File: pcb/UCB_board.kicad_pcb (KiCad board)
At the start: 4 copper layers, 160 x 100 mm, 141 parts, among them IC1 SN65HVD75DR, J1 DIN41612_02x32_AC, J2 TC2030, J3 Conn_01x02_Pin, T1 H1102NL, U1 W5500, U3 USBLC6-2SC6, U4 USBLC6-2SC6, U5 USBLC6-2SC6, U6 FM24C64B, U7 STM32H563VITx, Y1 3225-25M-SR, Y2 3225-25M-SR

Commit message: New power design
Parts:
- added C21: 10u, Capacitor_SMD:C_1206_3216Metric_Pad1.33x1.80mm_HandSolder, F.Cu at (205.9, 62.0)
- added C22: 10u, Capacitor_SMD:C_1206_3216Metric_Pad1.33x1.80mm_HandSolder, F.Cu at (210.9, 62.0)
- added C23: 100n, Capacitor_SMD:C_0603_1608Metric_Pad1.08x0.95mm_HandSolder, F.Cu at (195.8, 67.5)
- added C24: 100n, Capacitor_SMD:C_0603_1608Metric_Pad1.08x0.95mm_HandSolder, F.Cu at (197.3, 67.5)
- added C25: 10u, Capacitor_SMD:C_1206_3216Metric_Pad1.33x1.80mm_HandSolder, F.Cu at (190.7, 67.1)
- added C26: 100n, Capacitor_SMD:C_0603_1608Metric_Pad1.08x0.95mm_HandSolder, F.Cu at (195.1, 63.9)
- added D8: D_TVS, Diode_SMD:D_MiniMELF, B.Cu at (192.3, 62.0)
- added D9: ?, Diode_SMD:D_SMF, B.Cu at (191.9, 58.2)
- added F3: Polyfuse, Fuse:Fuse_1206_3216Metric_Pad1.42x1.75mm_HandSolder, B.Cu at (196.3, 58.3)
- C34: value 100n -> 10u; footprint Capacitor_SMD:C_0603_1608Metric_Pad1.08x0.95mm_HandSolder -> Capacitor_SMD:C_1206_3216Metric_Pad1.33x1.80mm_HandSolder
- D10, D11, D12, F2: moved to B.Cu
- L1: value B82464P4105M000 -> LQH32PN101MN0L; footprint Inductor_SMD:L_10.4x10.4_H4.8 -> Inductor_SMD:L_1210_3225Metric
- moved J2 37.7 mm to (212.5, 93.4)
- moved C33 27.3 mm to (191.8, 63.9), turned to 180 degrees
- moved C43 25.4 mm to (191.9, 58.1), turned to 90 degrees
- moved C42 19.0 mm to (217.2, 67.5), turned to 90 degrees
- moved C47 18.7 mm to (210.9, 59.6), turned to 180 degrees
- moved C48 18.3 mm to (215.8, 62.0), turned to 0 degrees
- moved L1 17.5 mm to (193.5, 66.9), turned to 90 degrees
- moved D10 17.4 mm to (211.7, 59.7), turned to 180 degrees
- moved C31 16.9 mm to (200.9, 62.0), turned to 180 degrees
- moved C41 16.9 mm to (215.7, 67.5), turned to 90 degrees
- moved C46 16.4 mm to (215.0, 63.9), turned to 0 degrees
- moved D11 16.4 mm to (200.9, 62.0), turned to 0 degrees
- moved F2 14.8 mm to (216.2, 58.3)
- moved C44 14.3 mm to (210.6, 67.1)
- moved L3 14.2 mm to (213.3, 66.9)
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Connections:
- C33 pad 1: Net-(C33-Pad1) -> Net-(D8-A2)
- C34 pad 1: Net-(C33-Pad1) -> Net-(D8-A2)
- C36 pad 1: Net-(C33-Pad1) -> Net-(D8-A2)
- C43 pad 1: +3.3V -> Net-(D8-A2)
- L1 pad 1: Net-(C33-Pad1) -> +12V
- L1 pad 2: Net-(D11-A2) -> Net-(D8-A2)
- L2 pad 2: Net-(C33-Pad1) -> Net-(D11-A2)
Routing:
- net /ConnectorDIN41612/PSU/+5V_IN: track 0.00 -> 37.8 mm, vias 0 -> 5
- net /ConnectorDIN41612/PSU/+12V_IN: track 0.00 -> 36.4 mm, vias 0 -> 5
- net /ConnectorDIN41612/PSU/+3,3V_IN: track 0.00 -> 33.5 mm, vias 0 -> 5
- net /ConnectorDIN41612/PSU/-12V_IN: track 0.00 -> 5.08 mm
- net Net-(D8-A2): vias 0 -> 5
- net Net-(D11-A2): vias 0 -> 5
- net Net-(D10-K): vias 0 -> 5
- net GND: vias 11 -> 12
- added copper zone on B.Cu, net /ConnectorDIN41612/PSU/+12V_IN
- added copper zone on In1.Cu, net /ConnectorDIN41612/PSU/+12V_IN
- added copper zone on B.Cu, net /ConnectorDIN41612/PSU/+3,3V_IN
- added copper zone on In1.Cu, net /ConnectorDIN41612/PSU/+3,3V_IN
- added copper zone on B.Cu, net /ConnectorDIN41612/PSU/+5V_IN
- added copper zone on In1.Cu, net /ConnectorDIN41612/PSU/+5V_IN
- added copper zone on B.Cu, net Net-(D10-K)
- added copper zone on F.Cu, net Net-(D10-K)
- added copper zone on B.Cu, net Net-(D8-A2)
- added copper zone on F.Cu, net Net-(D8-A2)
- removed copper zone on F.Cu, net Net-(C33-Pad1)

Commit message: Update
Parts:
- C53: moved to B.Cu
- moved C35 65.8 mm to (193.5, 110.2), turned to 90 degrees
- moved C29 62.3 mm to (191.9, 96.2), turned to -90 degrees
- moved C27 56.2 mm to (197.9, 92.4), turned to 180 degrees
- moved C53 48.5 mm to (202.5, 93.6), turned to -90 degrees
- moved C54 47.5 mm to (209.6, 111.6), turned to 180 degrees
- moved C49 46.2 mm to (205.9, 92.5), turned to 180 degrees
- moved C55 45.6 mm to (209.6, 110.1), turned to 180 degrees
- moved C50 42.5 mm to (209.5, 94.1), turned to -90 degrees
- moved TP3 9.58 mm to (215.6, 104.2)
- moved TP4 4.93 mm to (211.8, 104.3)
- moved TP12 1.30 mm to (203.5, 113.6)
- moved R91 1.02 mm to (211.8, 101.8)
- moved C20 0.05 mm to (199.5, 89.9)
- moved R20 0.05 mm to (201.7, 92.5)
- moved C19 0.05 mm to (204.0, 89.9)
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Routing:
- net GND: track 29.9 -> 58.5 mm, vias 12 -> 15
- net +3.3V: track 31.3 -> 59.3 mm, vias 16 -> 19
- net /MCU/nRESET: track 0.00 -> 23.4 mm, vias 0 -> 2
- net /MCU/SWDIO: track 0.00 -> 21.7 mm, vias 0 -> 2
- net /MCU/SWCLK: track 0.00 -> 20.5 mm, vias 0 -> 2
- net /MCU/SWO: track 0.00 -> 12.2 mm, vias 0 -> 2
- net /MCU/BOOT: track 0.00 -> 10.4 mm
- net /MCU/XTAL-: track 0.00 -> 6.00 mm
- net /MCU/XTAL+: track 0.00 -> 5.99 mm
- net /ConnectorDIN41612/RxD: track 4.99 -> 6.61 mm
- net /MCU/SDA: track 0.00 -> 1.35 mm, vias 0 -> 1
- net /ConnectorDIN41612/TxD: track 12.5 -> 13.3 mm, vias 0 -> 1

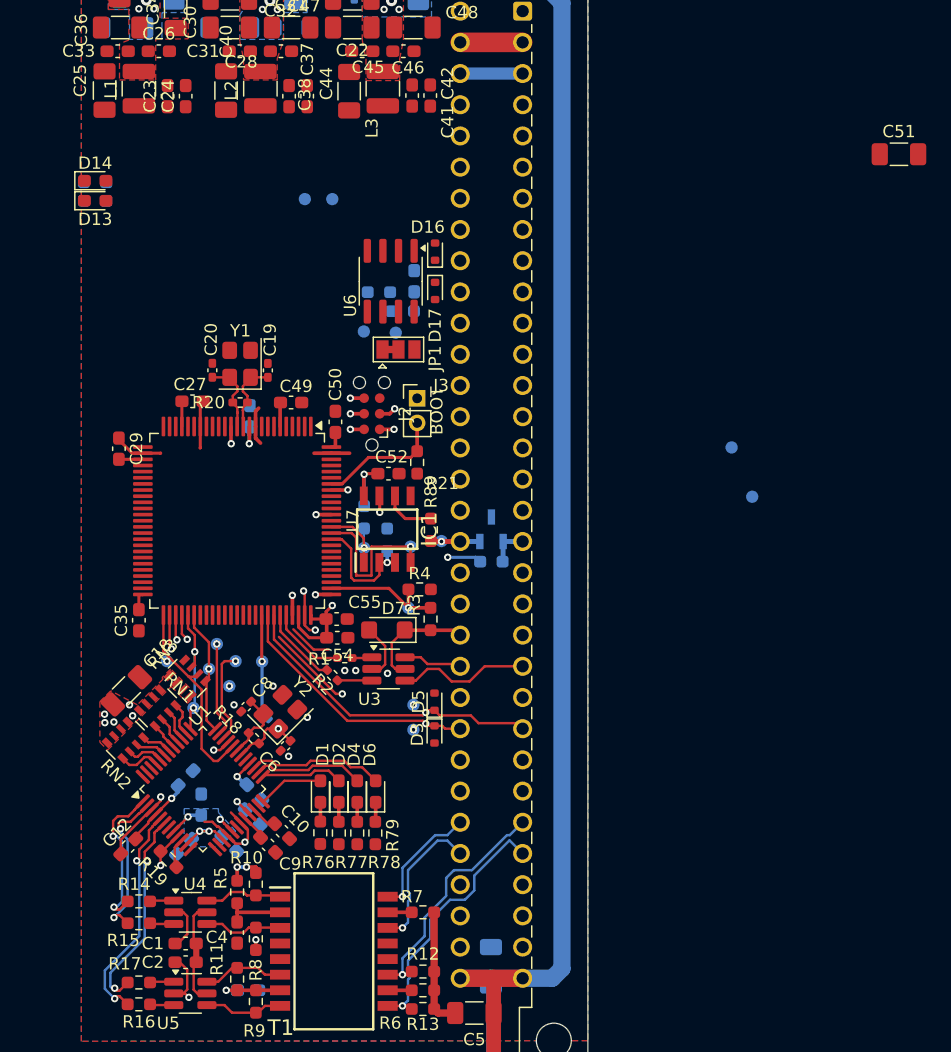
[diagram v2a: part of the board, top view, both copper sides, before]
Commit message: Add connections and new footprints
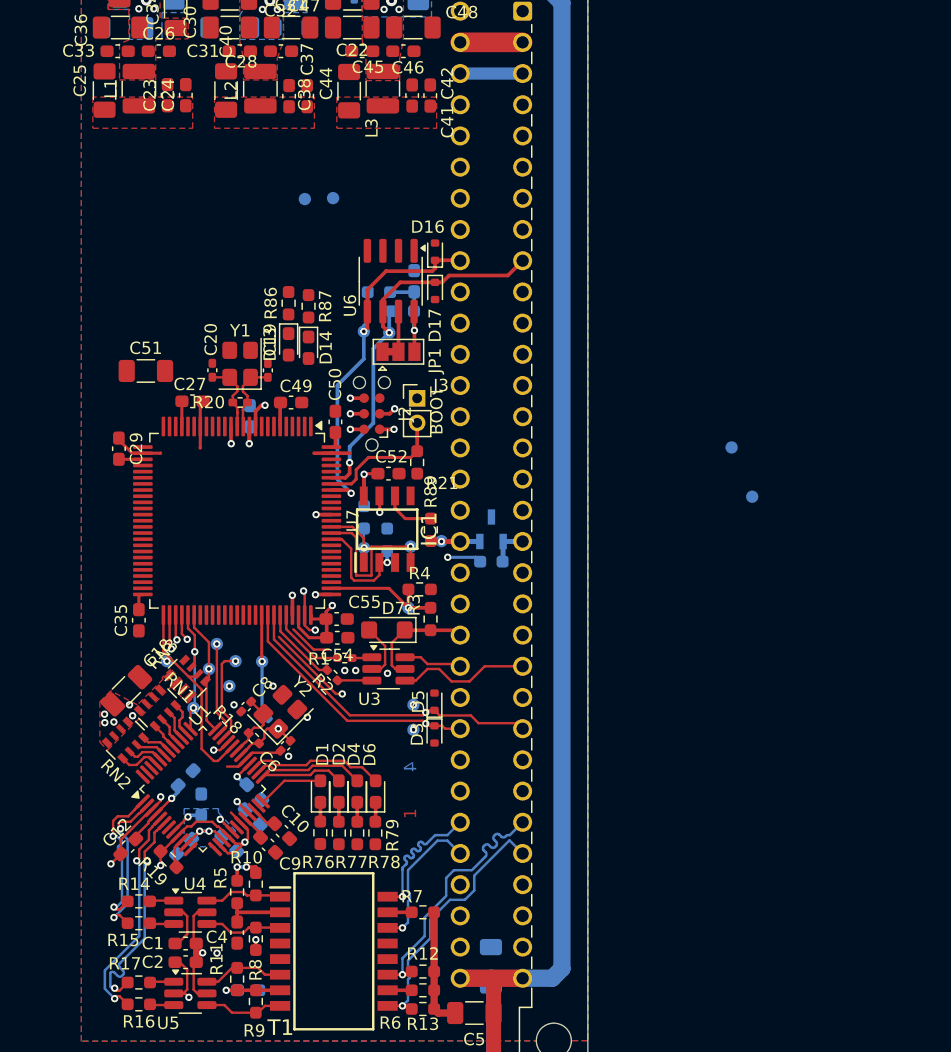
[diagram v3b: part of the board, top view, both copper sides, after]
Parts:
- added REF**: LayerMarker_4_6.35x2.54mm_TextH1mm_P1.27mm_LowerMirrored, Symbol:LayerMarker_4_6.35x2.54mm_TextH1mm_P1.27mm_LowerMirrored, F.Cu at (216.9, 126.0)
- R86, R87: moved to F.Cu
- moved C51 63.8 mm to (194.1, 89.9)
- moved D14 22.1 mm to (207.3, 88.0), turned to -90 degrees
- moved R87 20.1 mm to (207.3, 84.7), turned to 90 degrees
- moved D13 19.6 mm to (205.7, 87.8), turned to -90 degrees
- moved R86 17.8 mm to (205.7, 84.4), turned to 90 degrees
- moved TP8 0.53 mm to (213.9, 86.8)
- moved JP1 0.18 mm to (214.6, 88.4)
- moved TP21 0.10 mm to (209.3, 75.8)
- moved C24 0.08 mm to (197.3, 67.5)
- moved C23 0.08 mm to (195.8, 67.5)
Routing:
- net /MCU/SCL: track 0.00 -> 31.9 mm, vias 0 -> 2
- net /MCU/SDA: track 1.35 -> 32.0 mm, vias 1 -> 2
- net GND: track 58.5 -> 69.1 mm, vias 15 -> 18
- net +3.3V: track 59.3 -> 67.7 mm, vias 19 -> 20
- net Net-(JP1-C): track 0.00 -> 3.27 mm
- net /ConnectorDIN41612/TX+: track 9.80 -> 11.8 mm
- net /ConnectorDIN41612/RX+: track 19.5 -> 21.4 mm
- net /EthernetPHY/RXP: track 17.1 -> 18.4 mm
- net /MCU/nRESET: track 23.4 -> 22.7 mm
- net +5V: track 8.59 -> 9.11 mm, vias 0 -> 1
- added copper zone on F.Cu, net +12V
- added copper zone on F.Cu, net +5V

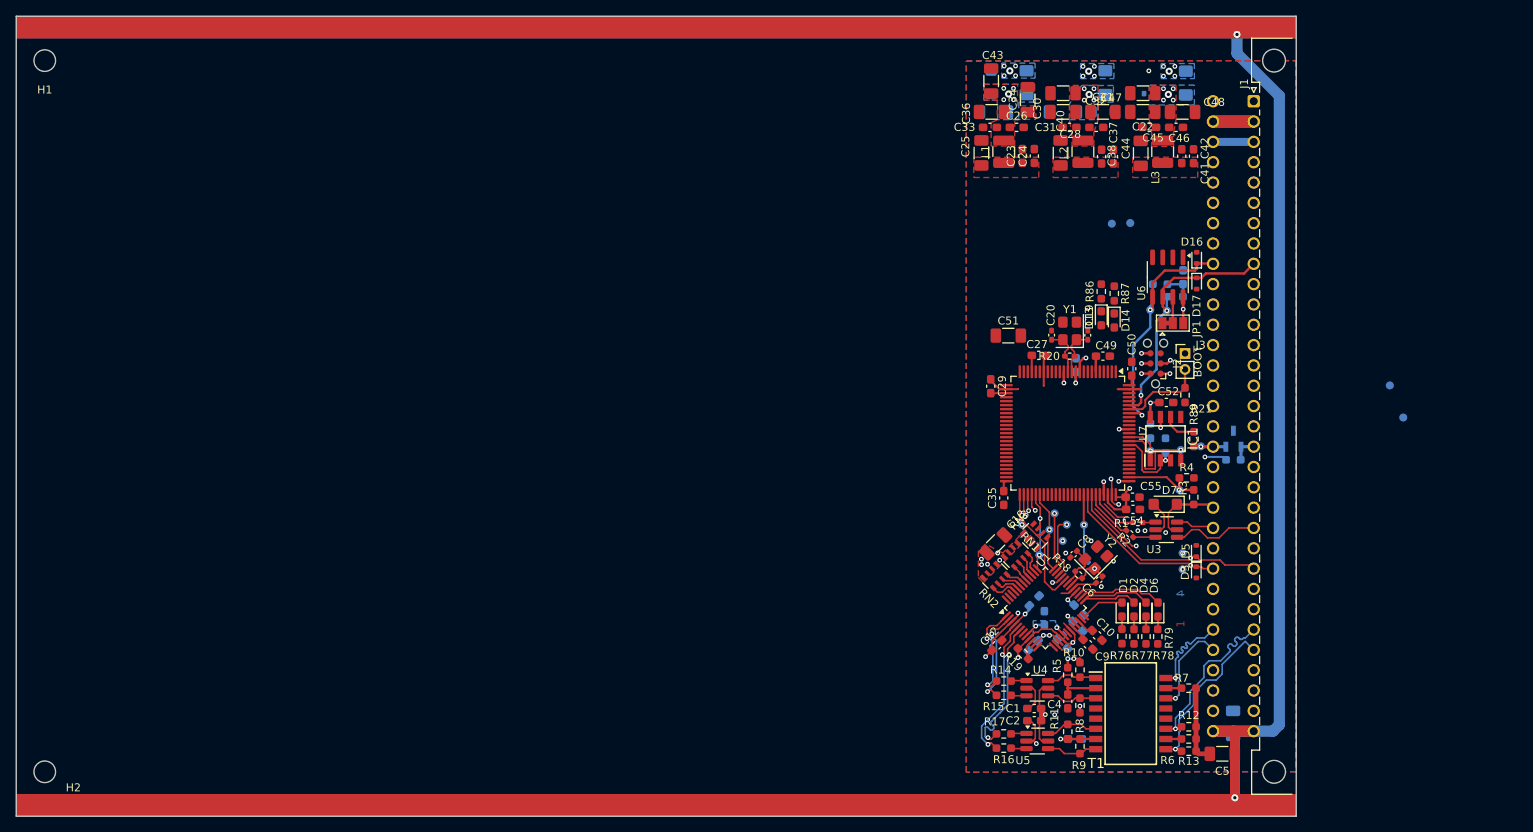
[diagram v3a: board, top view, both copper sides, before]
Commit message: Add UniConnector for io expansion (2.0mm pinheader)
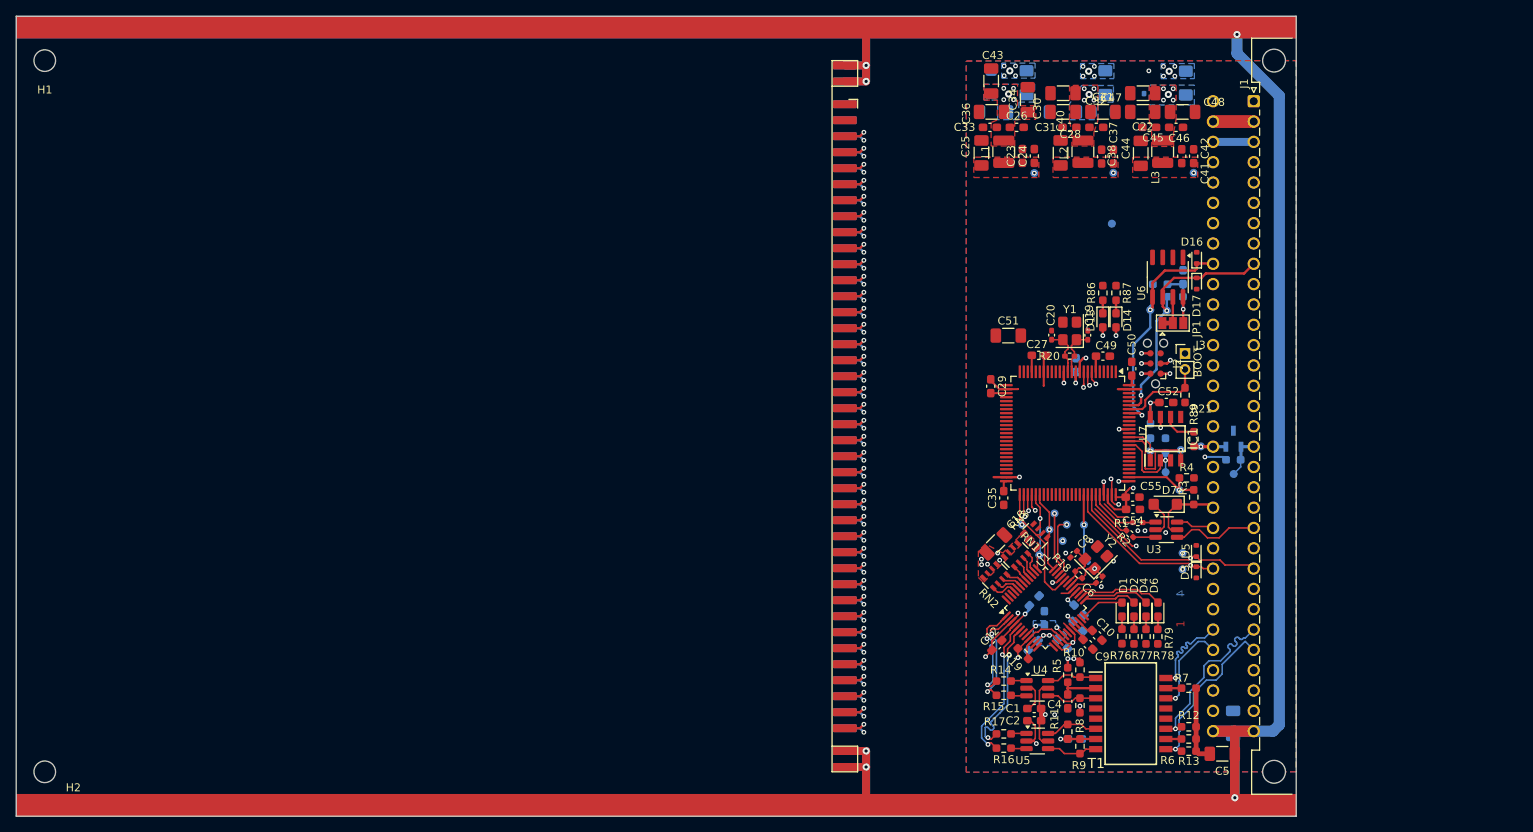
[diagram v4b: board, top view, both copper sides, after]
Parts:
- added TP10: TestPoint, TestPoint:TestPoint_Pad_D1.0mm, B.Cu at (197.3, 69.6)
- added TP9: TestPoint, TestPoint:TestPoint_Pad_D1.0mm, B.Cu at (207.2, 69.6)
- added X1: ~, Connector:UniConnector, F.Cu at (172.1, 100.0)
- moved TP2 30.5 mm to (213.7, 107.0)
- moved TP19 22.4 mm to (222.2, 107.2)
- moved TP21 10.1 mm to (217.2, 69.6)
- moved D13 0.32 mm to (205.9, 88.0)
- moved R86 0.26 mm to (205.9, 84.6)
- moved R87 0.23 mm to (207.5, 84.6)
- moved D14 0.22 mm to (207.5, 88.0)
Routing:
- net Earth: track 118.9 -> 272.2 mm, vias 2 -> 6
- net /MCU/LED_G: track 0.00 -> 10.5 mm, vias 0 -> 2
- net /MCU/LED_R: track 0.00 -> 10.5 mm, vias 0 -> 2
- net GND: track 69.1 -> 72.3 mm, vias 18 -> 19
- net /UniConnector/IO_8: track 0.00 -> 2.59 mm, vias 0 -> 1
- net /UniConnector/IO_64: track 0.00 -> 2.59 mm, vias 0 -> 1
- net /UniConnector/IO_62: track 0.00 -> 2.59 mm, vias 0 -> 1
- net /UniConnector/IO_60: track 0.00 -> 2.59 mm, vias 0 -> 1
- net /UniConnector/IO_6: track 0.00 -> 2.59 mm, vias 0 -> 1
- net /UniConnector/IO_58: track 0.00 -> 2.59 mm, vias 0 -> 1
- net /UniConnector/IO_56: track 0.00 -> 2.59 mm, vias 0 -> 1
- net /UniConnector/IO_54: track 0.00 -> 2.59 mm, vias 0 -> 1
- net /UniConnector/IO_52: track 0.00 -> 2.59 mm, vias 0 -> 1
- net /UniConnector/IO_50: track 0.00 -> 2.59 mm, vias 0 -> 1
- net /UniConnector/IO_48: track 0.00 -> 2.59 mm, vias 0 -> 1
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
